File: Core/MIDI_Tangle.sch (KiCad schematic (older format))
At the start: 32 parts, among them J1 USB_C_Receptacle_USB2.0, J2 Conn_01x04, J4 Conn_01x06_Male, J5 Conn_01x08_Female, J6 Conn_01x08_Female, J7 Conn_01x08_Female, J8 Conn_01x08_Female, SW1 SW_Push_DPDT, U1 ATSAMD21G15B-A, U14 MCP2517FD-xSL, U15 TLE9250V, Y1 20MHz

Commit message: Update termination
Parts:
- C41: value 22nF -> 4.7nF
- J1: symbol MIDI_Tangle-rescue:USB_C_Receptacle_USB2.0-Connector -> Connector:USB_C_Receptacle_USB2.0
- R11, R12: value 120 -> 56
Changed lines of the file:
@@
 	9950 5250 9950 5300
 $Comp
-L MIDI_Tangle-rescue:USB_C_Receptacle_USB2.0-Connector J1
+L Connector:USB_C_Receptacle_USB2.0 J1
 U 1 1 60EF2ED9
 P 1200 1450
@@
 P 6150 7000
 F 0 "R12" H 6220 7046 50  0000 L CNN
-F 1 "120" H 6220 6955 50  0000 L CNN
+F 1 "56" H 6220 6955 50  0000 L CNN
 F 2 "Resistor_SMD:R_0603_1608Metric" V 6080 7000 50  0001 C CNN
 F 3 "~" H 6150 7000 50  0001 C CNN
@@
 P 6150 7400
 F 0 "R11" H 6220 7446 50  0000 L CNN
-F 1 "120" H 6220 7355 50  0000 L CNN
+F 1 "56" H 6220 7355 50  0000 L CNN
 F 2 "Resistor_SMD:R_0603_1608Metric" V 6080 7400 50  0001 C CNN
 F 3 "~" H 6150 7400 50  0001 C CNN
@@
 P 6550 7200
 F 0 "C41" H 6665 7246 50  0000 L CNN
-F 1 "22nF" H 6665 7155 50  0000 L CNN
+F 1 "4.7nF" H 6665 7155 50  0000 L CNN
 F 2 "Capacitor_SMD:C_0603_1608Metric" H 6588 7050 50  0001 C CNN
 F 3 "~" H 6550 7200 50  0001 C CNN

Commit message: Add custom footprints and symbols
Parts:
- J1: footprint CustomLib:USB_C_Receptacle_GCT_USB4085_Slimmed -> Custom_FP:USB_C_Receptacle_GCT_USB4085_Slimmed
- J2: footprint CustomLib:MicroMatch_04_Vertical_SMD -> Custom_FP:MicroMatch_04_Vertical_SMD
- SW1: footprint CustomLib:SlideDPDT_JS202011 -> Custom_FP:SlideDPDT_JS202011
- Y1: footprint CustomLib:Crystal_2pin_2.0x2.5mm -> Custom_FP:Crystal_2pin_2.0x2.5mm
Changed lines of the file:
@@
 F 0 "J1" H 1307 2317 50  0000 C CNN
 F 1 "USB_C_Receptacle_USB2.0" H 1307 2226 50  0000 C CNN
-F 2 "CustomLib:USB_C_Receptacle_GCT_USB4085_Slimmed" H 1350 1450 50  0001 C CNN
+F 2 "Custom_FP:USB_C_Receptacle_GCT_USB4085_Slimmed" H 1350 1450 50  0001 C CNN
 F 3 "https://www.usb.org/sites/default/files/documents/usb_type-c.zip" H 1350 1450 50  0001 C CNN
 	1    1200 1450
@@
 F 0 "SW1" H 5700 7785 50  0000 C CNN
 F 1 "SW_Push_DPDT" H 5700 7694 50  0000 C CNN
-F 2 "CustomLib:SlideDPDT_JS202011" H 5700 7500 50  0001 C CNN
+F 2 "Custom_FP:SlideDPDT_JS202011" H 5700 7500 50  0001 C CNN
 F 3 "~" H 5700 7500 50  0001 C CNN
 	1    5700 7300
@@
 F 0 "J2" H 6080 4892 50  0000 L CNN
 F 1 "Conn_01x04" H 6080 4801 50  0000 L CNN
-F 2 "CustomLib:MicroMatch_04_Vertical_SMD" H 6000 4900 50  0001 C CNN
+F 2 "Custom_FP:MicroMatch_04_Vertical_SMD" H 6000 4900 50  0001 C CNN
 F 3 "~" H 6000 4900 50  0001 C CNN
 	1    6000 4900
@@
 F 0 "Y1" V 1754 6631 50  0000 L CNN
 F 1 "20MHz" V 1845 6631 50  0000 L CNN
-F 2 "CustomLib:Crystal_2pin_2.0x2.5mm" H 1800 6500 50  0001 C CNN
+F 2 "Custom_FP:Crystal_2pin_2.0x2.5mm" H 1800 6500 50  0001 C CNN
 F 3 "~" H 1800 6500 50  0001 C CNN
 	1    1800 6500

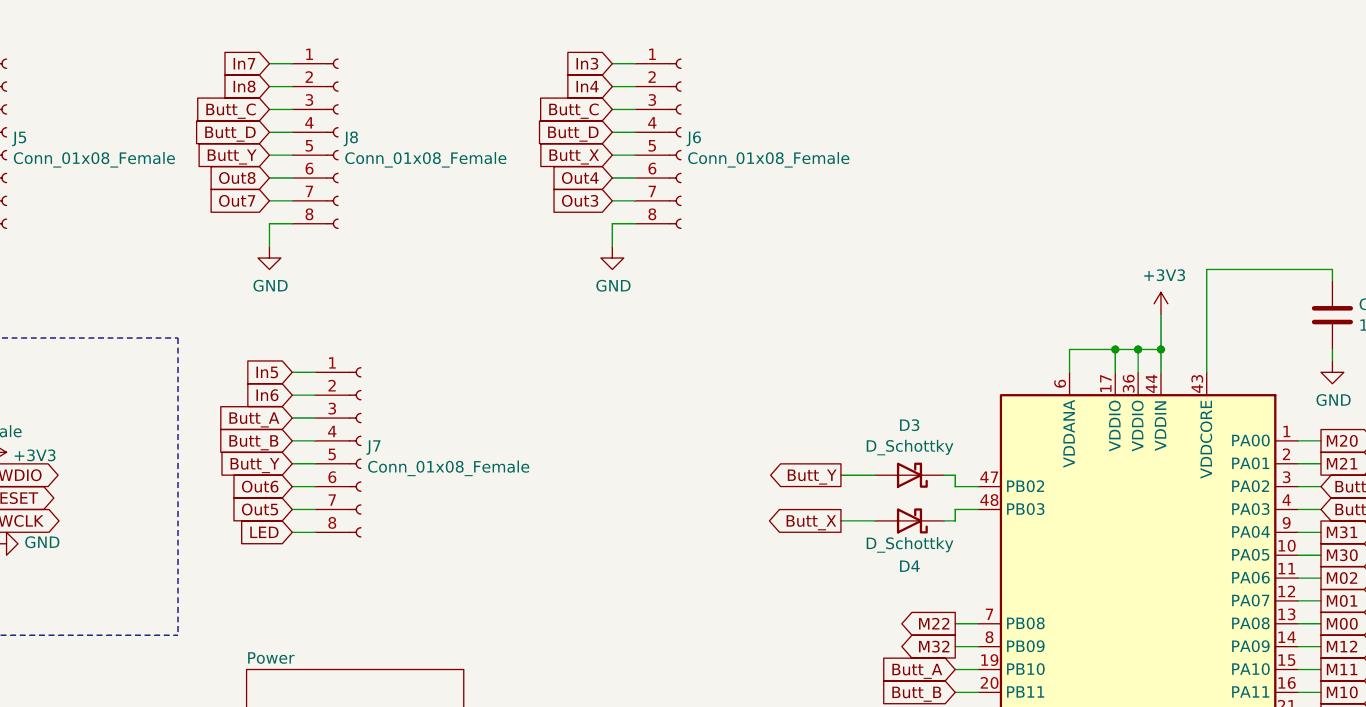
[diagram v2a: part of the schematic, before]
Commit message: Re-wire duplicate button signals
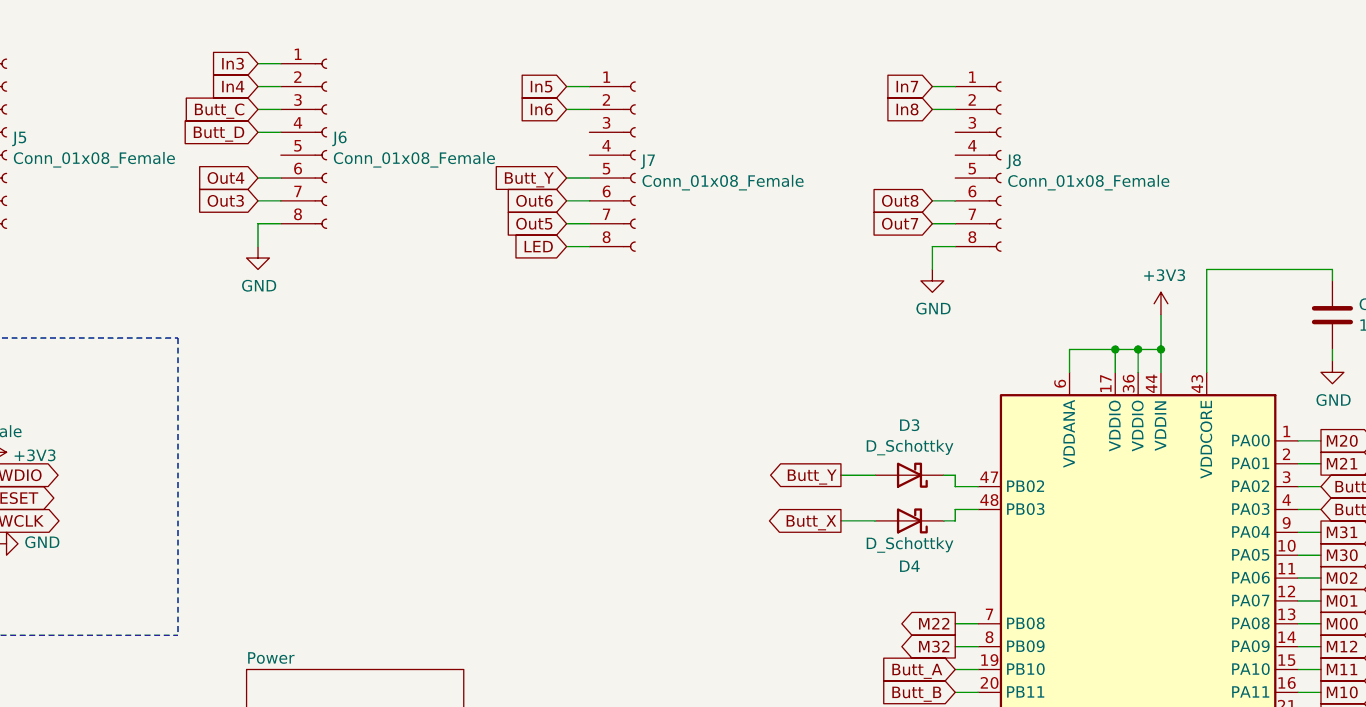
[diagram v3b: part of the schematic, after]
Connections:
- net Butt_A: no longer J7.3 (Pin_3)
- net Butt_B: no longer J7.4 (Pin_4)
- net Butt_C: no longer J8.3 (Pin_3)
- net Butt_D: no longer J8.4 (Pin_4)
- net Butt_X: no longer J6.5 (Pin_5)
- net Butt_Y: no longer J8.5 (Pin_5)
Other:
- moved on the sheet: J6, J7, J8
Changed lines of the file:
@@
 L Connector:Conn_01x08_Female J?
 U 1 1 60F7789C
-P 6500 1000
+P 4950 1000
 AR Path="/60AC3432/60F7789C" Ref="J?"  Part="1"
 AR Path="/60F7789C" Ref="J6"  Part="1"
-F 0 "J6" H 6528 976 50  0000 L CNN
-F 1 "Conn_01x08_Female" H 6528 885 50  0000 L CNN
-F 2 "Connector_PinSocket_2.54mm:PinSocket_1x08_P2.54mm_Vertical_SMD_Pin1Left" H 6500 1000 50  0001 C CNN
-F 3 "~" H 6500 1000 50  0001 C CNN
-	1    6500 1000
-	1    0    0    -1
-$EndComp
-Text GLabel 6200 700  0    50   Input ~ 0
+F 0 "J6" H 4978 976 50  0000 L CNN
+F 1 "Conn_01x08_Female" H 4978 885 50  0000 L CNN
+F 2 "Connector_PinSocket_2.54mm:PinSocket_1x08_P2.54mm_Vertical_SMD_Pin1Left" H 4950 1000 50  0001 C CNN
+F 3 "~" H 4950 1000 50  0001 C CNN
+	1    4950 1000
+	1    0    0    -1
+$EndComp
+Text GLabel 4650 700  0    50   Input ~ 0
 In3
-Text GLabel 6200 800  0    50   Input ~ 0
+Text GLabel 4650 800  0    50   Input ~ 0
 In4
-Text GLabel 6200 900  0    50   Input ~ 0
+Text GLabel 4650 900  0    50   Input ~ 0
 Butt_C
-Text GLabel 6200 1000 0    50   Input ~ 0
+Text GLabel 4650 1000 0    50   Input ~ 0
 Butt_D
-Text GLabel 6200 1100 0    50   Input ~ 0
-Butt_X
-Text GLabel 6200 1200 0    50   Input ~ 0
+Text GLabel 4650 1200 0    50   Input ~ 0
 Out4
-Text GLabel 6200 1300 0    50   Input ~ 0
+Text GLabel 4650 1300 0    50   Input ~ 0
 Out3
 $Comp
 L power:GND #PWR?
 U 1 1 60F778A9
-P 6200 1500
+P 4650 1500
 AR Path="/60AC3432/60F778A9" Ref="#PWR?"  Part="1"
 AR Path="/60F778A9" Ref="#PWR0114"  Part="1"
-F 0 "#PWR0114" H 6200 1250 50  0001 C CNN
-F 1 "GND" H 6205 1327 50  0000 C CNN
-F 2 "" H 6200 1500 50  0001 C CNN
-F 3 "" H 6200 1500 50  0001 C CNN
-	1    6200 1500
-	1    0    0    -1
-$EndComp
-Wire Wire Line
-	6200 1500 6200 1400
-Wire Wire Line
-	6200 1400 6300 1400
-Wire Wire Line
-	6300 1300 6200 1300
-Wire Wire Line
-	6200 1200 6300 1200
-Wire Wire Line
-	6300 1100 6200 1100
-Wire Wire Line
-	6200 1000 6300 1000
-Wire Wire Line
-	6300 900  6200 900
-Wire Wire Line
-	6200 800  6300 800
-Wire Wire Line
-	6300 700  6200 700
+F 0 "#PWR0114" H 4650 1250 50  0001 C CNN
+F 1 "GND" H 4655 1327 50  0000 C CNN
+F 2 "" H 4650 1500 50  0001 C CNN
+F 3 "" H 4650 1500 50  0001 C CNN
+	1    4650 1500
+	1    0    0    -1
+$EndComp
+Wire Wire Line
+	4650 1500 4650 1400
+Wire Wire Line
+	4650 1400 4750 1400
+Wire Wire Line
+	4750 1300 4650 1300
+Wire Wire Line
+	4650 1200 4750 1200
+Wire Wire Line
+	4650 1000 4750 1000
+Wire Wire Line
+	4750 900  4650 900
+Wire Wire Line
+	4650 800  4750 800
+Wire Wire Line
+	4750 700  4650 700
 $Comp
 L Connector:Conn_01x08_Female J?
 U 1 1 60F778B8
-P 5100 2350
+P 6300 1100
 AR Path="/60AC3432/60F778B8" Ref="J?"  Part="1"
 AR Path="/60F778B8" Ref="J7"  Part="1"
-F 0 "J7" H 5128 2326 50  0000 L CNN
-F 1 "Conn_01x08_Female" H 5128 2235 50  0000 L CNN
-F 2 "Connector_PinSocket_2.54mm:PinSocket_1x08_P2.54mm_Vertical_SMD_Pin1Left" H 5100 2350 50  0001 C CNN
-F 3 "~" H 5100 2350 50  0001 C CNN
-	1    5100 2350
-	1    0    0    -1
-$EndComp
-Text GLabel 4800 2050 0    50   Input ~ 0
+F 0 "J7" H 6328 1076 50  0000 L CNN
+F 1 "Conn_01x08_Female" H 6328 985 50  0000 L CNN
+F 2 "Connector_PinSocket_2.54mm:PinSocket_1x08_P2.54mm_Vertical_SMD_Pin1Left" H 6300 1100 50  0001 C CNN
+F 3 "~" H 6300 1100 50  0001 C CNN
+	1    6300 1100
+	1    0    0    -1
+$EndComp
+Text GLabel 6000 800  0    50   Input ~ 0
 In5
-Text GLabel 4800 2150 0    50   Input ~ 0
+Text GLabel 6000 900  0    50   Input ~ 0
 In6
-Text GLabel 4800 2250 0    50   Input ~ 0
-Butt_A
-Text GLabel 4800 2350 0    50   Input ~ 0
-Butt_B
-Text GLabel 4800 2450 0    50   Input ~ 0
-Butt_Y
-Text GLabel 4800 2550 0    50   Input ~ 0
+Text GLabel 6000 1300 0    50   Input ~ 0
 Out6
-Text GLabel 4800 2650 0    50   Input ~ 0
+Text GLabel 6000 1400 0    50   Input ~ 0
 Out5
 Wire Wire Line
-	4900 2650 4800 2650
-Wire Wire Line
-	4800 2550 4900 2550
-Wire Wire Line
-	4900 2450 4800 2450
-Wire Wire Line
-	4800 2350 4900 2350
-Wire Wire Line
-	4900 2250 4800 2250
-Wire Wire Line
-	4800 2150 4900 2150
-Wire Wire Line
-	4900 2050 4800 2050
+	6100 1400 6000 1400
+Wire Wire Line
+	6000 1300 6100 1300
+Wire Wire Line
+	6000 900  6100 900
+Wire Wire Line
+	6100 800  6000 800
 $Comp
 L Connector:Conn_01x08_Female J?
 U 1 1 60F778CC
-P 5000 1000
+P 7900 1100
 AR Path="/60AC3432/60F778CC" Ref="J?"  Part="1"
 AR Path="/60F778CC" Ref="J8"  Part="1"
-F 0 "J8" H 5028 976 50  0000 L CNN
-F 1 "Conn_01x08_Female" H 5028 885 50  0000 L CNN
-F 2 "Connector_PinSocket_2.54mm:PinSocket_1x08_P2.54mm_Vertical_SMD_Pin1Left" H 5000 1000 50  0001 C CNN
-F 3 "~" H 5000 1000 50  0001 C CNN
-	1    5000 1000
-	1    0    0    -1
-$EndComp
-Text GLabel 4700 700  0    50   Input ~ 0
+F 0 "J8" H 7928 1076 50  0000 L CNN
+F 1 "Conn_01x08_Female" H 7928 985 50  0000 L CNN
+F 2 "Connector_PinSocket_2.54mm:PinSocket_1x08_P2.54mm_Vertical_SMD_Pin1Left" H 7900 1100 50  0001 C CNN
+F 3 "~" H 7900 1100 50  0001 C CNN
+	1    7900 1100
+	1    0    0    -1
+$EndComp
+Text GLabel 7600 800  0    50   Input ~ 0
 In7
-Text GLabel 4700 800  0    50   Input ~ 0
+Text GLabel 7600 900  0    50   Input ~ 0
 In8
-Text GLabel 4700 900  0    50   Input ~ 0
-Butt_C
-Text GLabel 4700 1000 0    50   Input ~ 0
-Butt_D
-Text GLabel 4700 1100 0    50   Input ~ 0
+Text GLabel 6000 1200 0    50   Input ~ 0
 Butt_Y
-Text GLabel 4700 1200 0    50   Input ~ 0
+Text GLabel 7600 1300 0    50   Input ~ 0
 Out8
-Text GLabel 4700 1300 0    50   Input ~ 0
+Text GLabel 7600 1400 0    50   Input ~ 0
 Out7
 $Comp
 L power:GND #PWR?
 U 1 1 60F778D9
-P 4700 1500
+P 7600 1600
 AR Path="/60AC3432/60F778D9" Ref="#PWR?"  Part="1"
 AR Path="/60F778D9" Ref="#PWR0115"  Part="1"
-F 0 "#PWR0115" H 4700 1250 50  0001 C CNN
-F 1 "GND" H 4705 1327 50  0000 C CNN
-F 2 "" H 4700 1500 50  0001 C CNN
-F 3 "" H 4700 1500 50  0001 C CNN
-	1    4700 1500
-	1    0    0    -1
-$EndComp
-Wire Wire Line
-	4700 1500 4700 1400
-Wire Wire Line
-	4700 1400 4800 1400
-Wire Wire Line
-	4800 1300 4700 1300
-Wire Wire Line
-	4700 1200 4800 1200
-Wire Wire Line
-	4800 1100 4700 1100
-Wire Wire Line
-	4700 1000 4800 1000
-Wire Wire Line
-	4800 900  4700 900
-Wire Wire Line
-	4700 800  4800 800
-Wire Wire Line
-	4800 700  4700 700
-Text GLabel 4800 2750 0    50   Input ~ 0
+F 0 "#PWR0115" H 7600 1350 50  0001 C CNN
+F 1 "GND" H 7605 1427 50  0000 C CNN
+F 2 "" H 7600 1600 50  0001 C CNN
+F 3 "" H 7600 1600 50  0001 C CNN
+	1    7600 1600
+	1    0    0    -1
+$EndComp
+Wire Wire Line
+	7600 1600 7600 1500
+Wire Wire Line
+	7600 1500 7700 1500
+Wire Wire Line
+	7700 1400 7600 1400
+Wire Wire Line
+	7600 1300 7700 1300
+Wire Wire Line
+	7600 900  7700 900
+Wire Wire Line
+	7700 800  7600 800
+Text GLabel 6000 1500 0    50   Input ~ 0
 LED
 Wire Wire Line
-	4800 2750 4900 2750
+	6000 1500 6100 1500
 Text GLabel 10250 800  0    50   Input ~ 0
 M01
@@
 Wire Wire Line
 	10650 4900 10650 4800
+Wire Wire Line
+	6000 1200 6100 1200
 $EndSCHEMATC

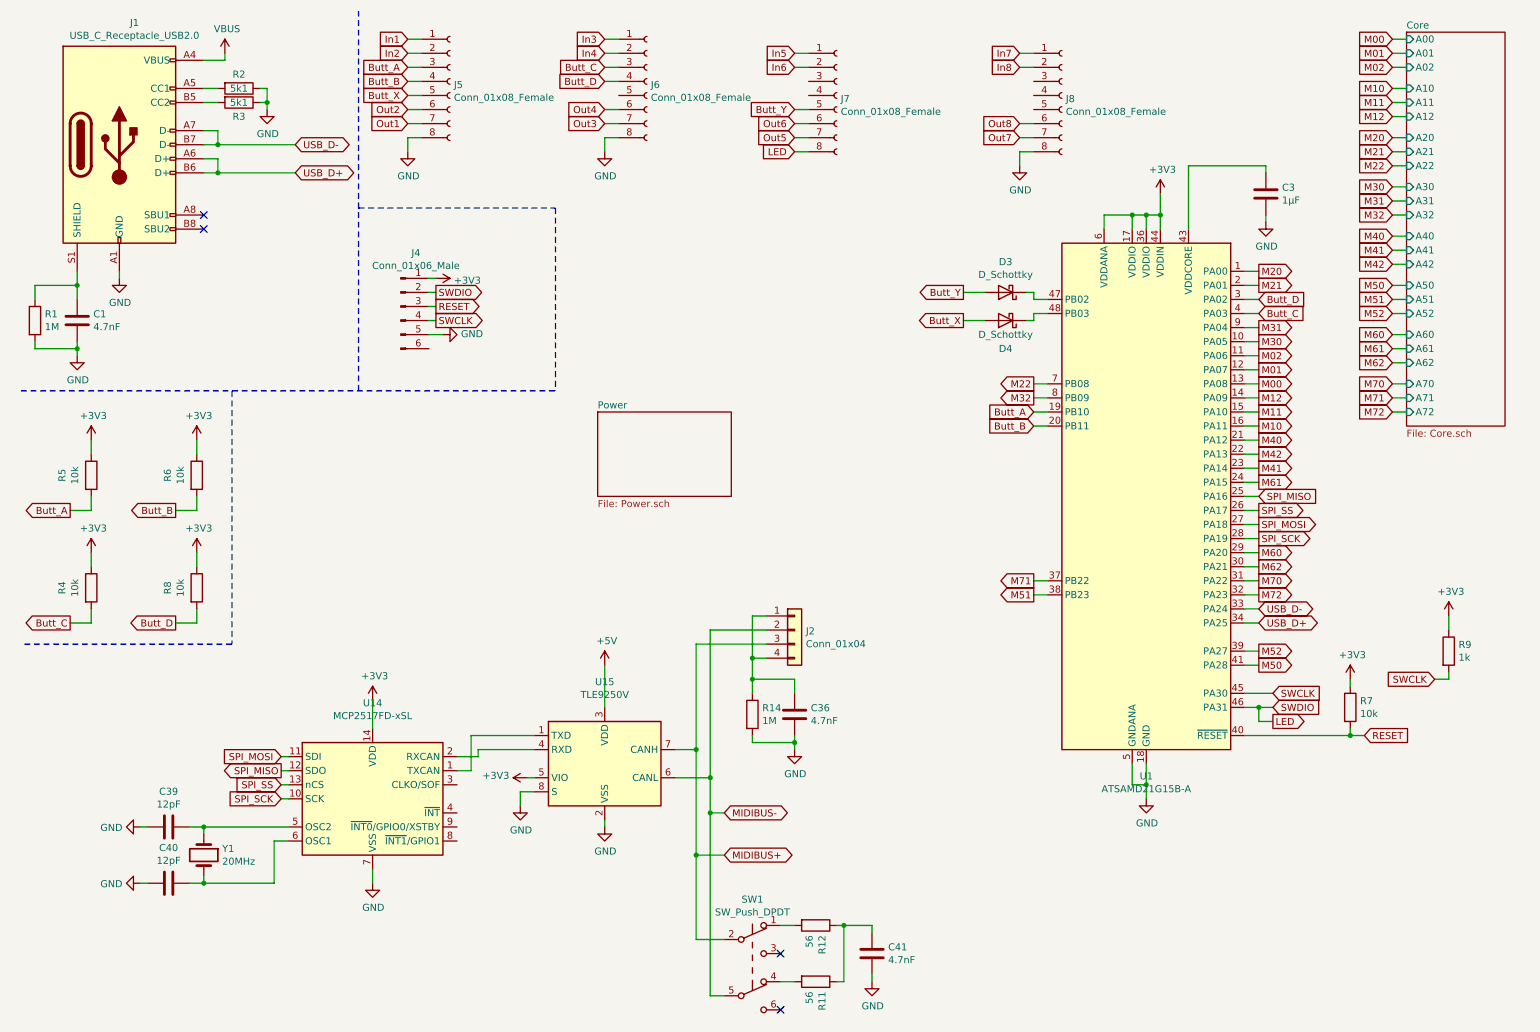
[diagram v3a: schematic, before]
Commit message: Add shift-registers+++
Added shift-registers
Added power protection
Changed USB footprint
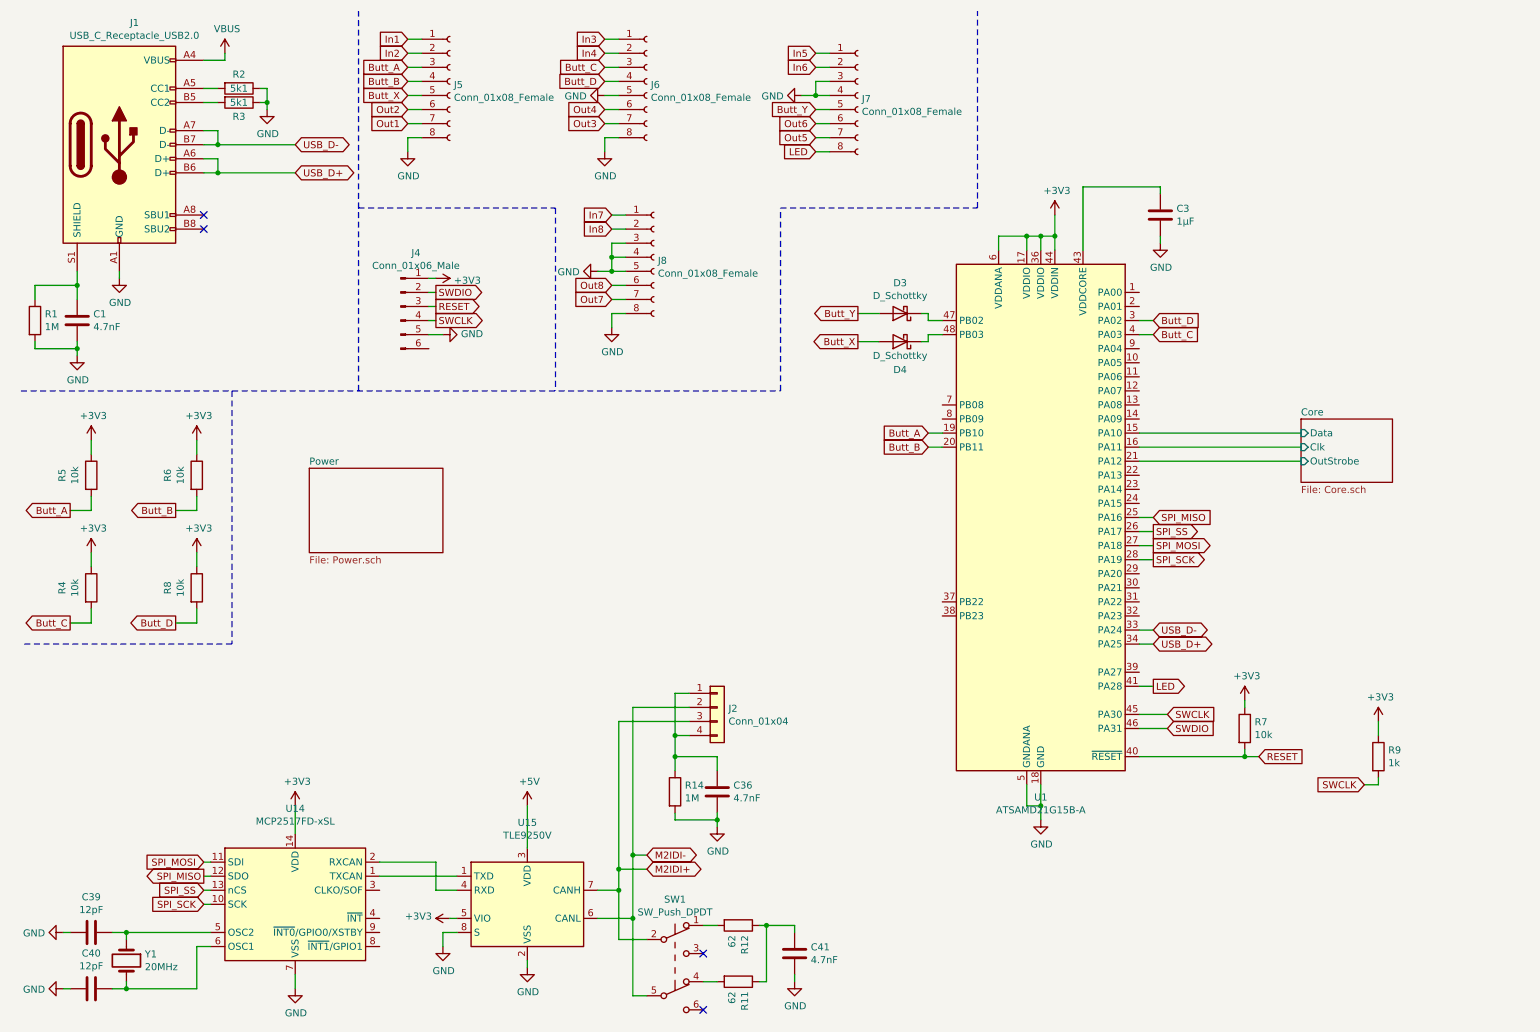
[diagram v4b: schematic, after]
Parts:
- J1: footprint Custom_FP:USB_C_Receptacle_GCT_USB4085_Slimmed -> Connector_USB:USB_C_Receptacle_HRO_TYPE-C-31-M-12
- R11, R12: value 56 -> 62
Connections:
- net M50 is gone; now on net LED: U1.41 (PA28)
- net GND: now also J6.5 (Pin_5), J7.3 (Pin_3), J7.4 (Pin_4), J8.3 (Pin_3), J8.4 (Pin_4), J8.5 (Pin_5)
- net LED: no longer J4.2 (Pin_2), U1.46 (PA31)
- net M00: no longer names the net of U1.13 (PA08)
- net M01: no longer names the net of U1.12 (PA07)
- net M02: no longer names the net of U1.11 (PA06)
- net M10 renamed Core/Clk
- net M11 renamed Core/Data
- net M12: no longer names the net of U1.14 (PA09)
- net M20: no longer names the net of U1.1 (PA00)
- net M21: no longer names the net of U1.2 (PA01)
- net M22: no longer names the net of U1.7 (PB08)
- net M30: no longer names the net of U1.10 (PA05)
- net M31: no longer names the net of U1.9 (PA04)
- net M32: no longer names the net of U1.8 (PB09)
- net M40 renamed Core/OutStrobe
- net M41: no longer names the net of U1.23 (PA14)
- net M42: no longer names the net of U1.22 (PA13)
- net M51: no longer names the net of U1.38 (PB23)
- net M52: no longer names the net of U1.39 (PA27)
- net M60: no longer names the net of U1.29 (PA20)
- net M61: no longer names the net of U1.24 (PA15)
- net M62: no longer names the net of U1.30 (PA21)
- net M70: no longer names the net of U1.31 (PA22)
- net M71: no longer names the net of U1.37 (PB22)
- net M72: no longer names the net of U1.32 (PA23)
- net MIDIBUS+ renamed M2IDI+
- net MIDIBUS- renamed M2IDI-
- new net SWDIO: J4.2 (Pin_2), U1.46 (PA31)
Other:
- moved on the sheet: C3, C36, C39, C40, C41, D3, D4, J2, J7, J8, R11, R12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
